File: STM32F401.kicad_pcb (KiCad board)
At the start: 4 copper layers, 50 x 50 mm, 32 parts, among them J1 Conn_02x10_Odd_Even, J2 Conn_02x10_Odd_Even, J3 POWER, J4 USB_B_Micro, J5 Conn_01x04, J6 Micro_SD_Card, U1 AMS1117-3.3, U2 STM32F401RCTx

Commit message: first commit
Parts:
- added ?: , , F.Cu at (115.3, 157.1)
- added ?: , , F.Cu at (115.3, 77.1)
- added ?: , , F.Cu at (201.0, 80.9)
- added ?: , , F.Cu at (201.0, 154.6)
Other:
- board size 50 x 50 mm -> 92.1 x 89.1 mm
- net class Default removed

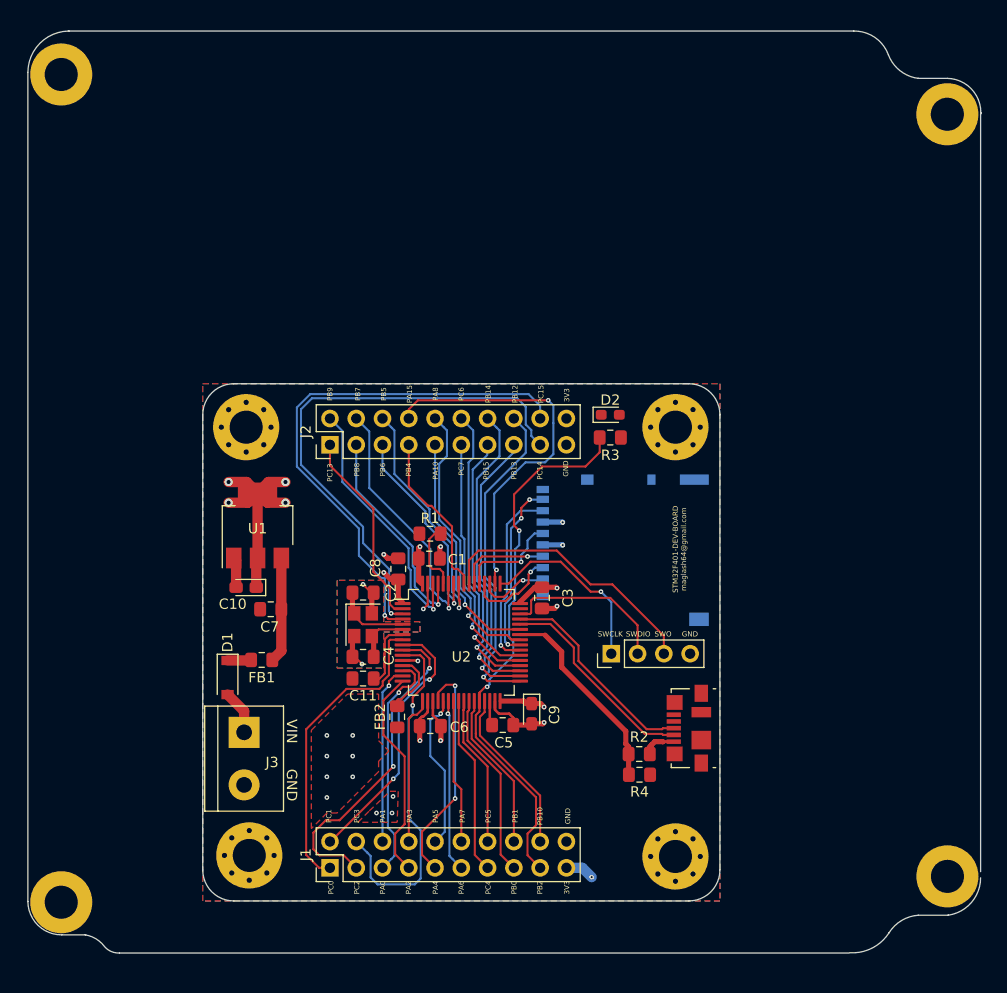
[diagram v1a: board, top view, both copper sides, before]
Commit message: modified PCB layout for a CubeSat board
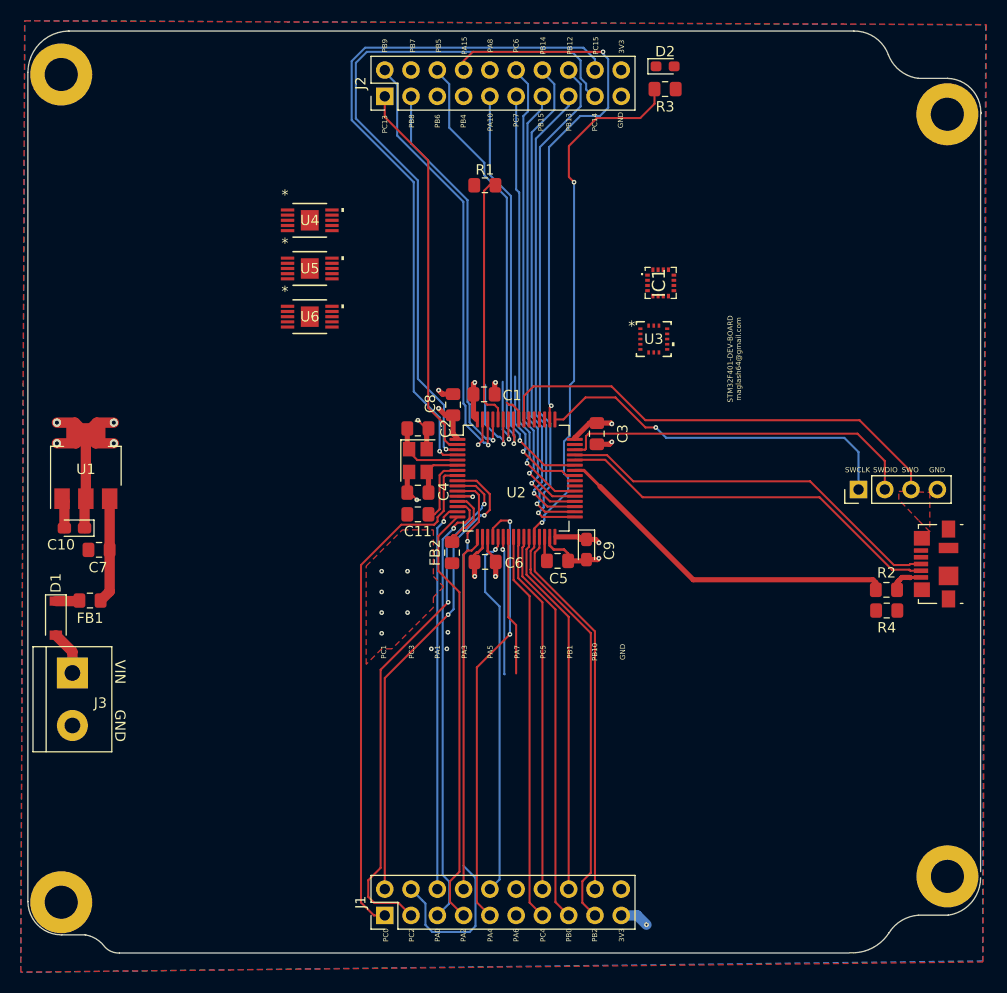
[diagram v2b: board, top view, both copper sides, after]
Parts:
- removed H1, H2, H3, H4: MountingHole_Pad, MountingHole:MountingHole_3.2mm_M3_Pad_Via
- removed J6: Micro_SD_Card, Connector_Card:microSD_HC_Hirose_DM3AT-SF-PEJM5
- added IC1: MMC5983MA, adcs-footprints:MMC5983MA, F.Cu at (173.3, 97.2)
- added U3: IAM-20380, adcs-footprints:IAM-20380_IVS, F.Cu at (172.6, 102.7)
- added U4: A3909GLYTR-T, adcs-footprints:A3909GLYTR-T_ALM, F.Cu at (139.3, 91.2)
- added U5: A3909GLYTR-T, adcs-footprints:A3909GLYTR-T_ALM, F.Cu at (139.3, 95.9)
- added U6: A3909GLYTR-T, adcs-footprints:A3909GLYTR-T_ALM, F.Cu at (139.3, 100.5)
- FB1, FB2: value 100 ohms -> 100 ohms
- moved J2 34.1 mm to (146.6, 79.2)
- moved R1 34.1 mm to (156.3, 87.8)
- moved D2 34.1 mm to (173.7, 76.3)
- moved R3 34.1 mm to (173.7, 78.5)
- moved J4 28.7 mm to (199.9, 124.4)
- moved R2 28.7 mm to (195.1, 126.9)
- moved R4 28.7 mm to (195.1, 128.9)
- moved J5 28.7 mm to (192.4, 117.2)
- moved D1 17.6 mm to (114.8, 129.7)
- moved U1 17.6 mm to (117.7, 115.0)
- moved C10 17.6 mm to (116.6, 121.0)
- moved C7 17.6 mm to (119.0, 123.1)
- moved FB1 17.6 mm to (118.1, 128.0)
- moved J3 17.6 mm to (116.4, 135.0)
- moved HSE1 16.7 mm to (149.8, 114.4)
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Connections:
- ? pad 0: (no net) -> GND (x3)
- ? pad 0: ESD -> GND
- J1 pad 11: PA6 -> unconnected-(J1-Pin_11-Pad11)
- J1 pad 12: PA7 -> unconnected-(J1-Pin_12-Pad12)
- J2 pad 10: PA8 -> unconnected-(J2-Pin_10-Pad10)
- J2 pad 4: PB7 -> unconnected-(J2-Pin_4-Pad4)
- J2 pad 5: PB6 -> unconnected-(J2-Pin_5-Pad5)
- J2 pad 7: PB4 -> unconnected-(J2-Pin_7-Pad7)
- J4 pad 4: Net-(J4-Pad4) -> unconnected-(J4-ID-Pad4)
- J4 pad 6: GND -> (no net)
- U2 pad 30: Net-(C5-Pad1) -> Net-(U2-VCAP1)
- U2 pad 39: SDIO_D0 -> unconnected-(U2-PC8-Pad39)
- U2 pad 40: SDIO_D1 -> unconnected-(U2-PC9-Pad40)
- U2 pad 41: PA8 -> I2C3_SCL
- U2 pad 51: SDIO_D2 -> unconnected-(U2-PC10-Pad51)
- U2 pad 52: SDIO_D3 -> unconnected-(U2-PC11-Pad52)
- U2 pad 53: SDIO_CLK -> unconnected-(U2-PC12-Pad53)
- U2 pad 54: SDIO_CMD -> unconnected-(U2-PD2-Pad54)
- U2 pad 56: PB4 -> I2C3_SDA
- U2 pad 58: PB6 -> I2C1_SCL
- U2 pad 59: PB7 -> I2C1_SDA
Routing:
- net PB2: track 53.1 -> 91.4 mm
- net PA8: track 27.2 -> 0.00 mm, vias 1 -> 0
- net PB7: track 24.6 -> 0.00 mm, vias 1 -> 0
- net PC1: track 25.8 -> 46.3 mm
- net PC5: track 14.6 -> 35.0 mm
- net PB10: track 16.2 -> 36.7 mm
- net PA3: track 14.4 -> 34.8 mm
- net PA1: track 17.3 -> 37.8 mm
- net PB1: track 15.4 -> 35.9 mm
- net PA0: track 22.3 -> 42.7 mm
- net PC4: track 17.3 -> 37.8 mm
- net PA5: track 15.3 -> 35.8 mm
- net PC0: track 30.1 -> 50.5 mm
- net PB0: track 18.0 -> 38.5 mm
- net PA2: track 20.6 -> 41.1 mm
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- added copper zone on F.Cu, net +3V3
- removed copper zone on In2.Cu, net +3V3
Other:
- outline, holes or cut-outs redrawn
